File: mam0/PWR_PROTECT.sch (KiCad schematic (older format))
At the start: 4 parts

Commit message: готова схема, требуется проверка
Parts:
- added C? (x4): Конденсатор_керамический, N_RLC:Конденсатор_SMD_0603, symbol elements:Конденсатор_керамический
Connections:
- net GND_OUT: now also C?.2, C?.2, C?.2, C?.2
- net V_OUT: now also C?.1, C?.1, C?.1, C?.1
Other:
- note added: "На интерфейс RS485"
- note added: "На микроконтроллер (AVCC)"
- note added: "На микроконтроллер (VCC)"
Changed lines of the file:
@@
 EESchema Schematic File Version 4
+LIBS:mam0-cache
 EELAYER 29 0
 EELAYER END
 $Descr A4 11693 8268
 encoding utf-8
-Sheet 2 2
+Sheet 2 3
 Title ""
 Date ""
@@
 Wire Wire Line
 	5750 3250 5750 3000
-Text HLabel 6250 2500 2    50   Input ~ 0
+Text HLabel 9000 2500 2    50   Input ~ 0
 V_OUT
 Wire Wire Line
-	5750 2500 6250 2500
+	5750 2500 6500 2500
 Connection ~ 5750 2500
-Text HLabel 6250 3250 2    50   Input ~ 0
+Text HLabel 9000 3250 2    50   Input ~ 0
 GND_OUT
-Wire Wire Line
-	6250 3250 5750 3250
 $Comp
 L elements:Предохранитель FU?
@@
 	4750 3250 4500 3250
 Connection ~ 4500 3250
+$Comp
+L elements:Конденсатор_керамический C?
+U 1 1 5DBC916F
+P 6500 2800
+AR Path="/5DBC916F" Ref="C?"  Part="1"
+AR Path="/5DB9AA7C/5DBC916F" Ref="C?"  Part="1"
+F 0 "C?" V 6450 2950 60  0000 C CNN
+F 1 "Конденсатор_керамический" H 6600 2700 60  0001 C CNN
+F 2 "N_RLC:Конденсатор_SMD_0603" H 6500 2800 60  0001 C CNN
+F 3 "" H 6500 2800 60  0001 C CNN
+F 4 "10 мкФ/6,3 В" V 6650 3100 50  0000 C CNN "Номинал"
+F 5 "С111" H 6500 2800 50  0001 C CNN "УГО"
+	1    6500 2800
+	0    1    1    0
+$EndComp
+$Comp
+L elements:Конденсатор_керамический C?
+U 1 1 5DBC91F5
+P 7250 2800
+AR Path="/5DBC91F5" Ref="C?"  Part="1"
+AR Path="/5DB9AA7C/5DBC91F5" Ref="C?"  Part="1"
+F 0 "C?" V 7200 2950 60  0000 C CNN
+F 1 "Конденсатор_керамический" H 7350 2700 60  0001 C CNN
+F 2 "N_RLC:Конденсатор_SMD_0603" H 7250 2800 60  0001 C CNN
+F 3 "" H 7250 2800 60  0001 C CNN
+F 4 "10 мкФ/6,3 В" V 7400 3100 50  0000 C CNN "Номинал"
+F 5 "С111" H 7250 2800 50  0001 C CNN "УГО"
+	1    7250 2800
+	0    1    1    0
+$EndComp
+Wire Wire Line
+	6500 2750 6500 2500
+Connection ~ 6500 2500
+Wire Wire Line
+	6500 2500 7250 2500
+Wire Wire Line
+	7250 2750 7250 2500
+Wire Wire Line
+	7250 2900 7250 3250
+Wire Wire Line
+	7250 3250 6500 3250
+Wire Wire Line
+	6500 2900 6500 3250
+Connection ~ 6500 3250
+Wire Wire Line
+	6500 3250 5750 3250
+Text Notes 6500 2450 1    50   ~ 0
+На микроконтроллер (VCC)
+Text Notes 7250 2450 1    50   ~ 0
+На микроконтроллер (VCC)
+Wire Wire Line
+	8750 2500 9000 2500
+Wire Wire Line
+	8750 3250 9000 3250
+$Comp
+L elements:Конденсатор_керамический C?
+U 1 1 5DC347F0
+P 8000 2800
+AR Path="/5DC347F0" Ref="C?"  Part="1"
+AR Path="/5DB9AA7C/5DC347F0" Ref="C?"  Part="1"
+F 0 "C?" V 7950 2950 60  0000 C CNN
+F 1 "Конденсатор_керамический" H 8100 2700 60  0001 C CNN
+F 2 "N_RLC:Конденсатор_SMD_0603" H 8000 2800 60  0001 C CNN
+F 3 "" H 8000 2800 60  0001 C CNN
+F 4 "10 мкФ/6,3 В" V 8150 3100 50  0000 C CNN "Номинал"
+F 5 "С111" H 8000 2800 50  0001 C CNN "УГО"
+	1    8000 2800
+	0    1    1    0
+$EndComp
+Wire Wire Line
+	8000 2750 8000 2500
+Wire Wire Line
+	8000 2900 8000 3250
+Wire Wire Line
+	8000 2500 7250 2500
+Connection ~ 7250 2500
+Wire Wire Line
+	7250 3250 8000 3250
+Connection ~ 7250 3250
+Text Notes 8000 2450 1    50   ~ 0
+На микроконтроллер (AVCC)
+$Comp
+L elements:Конденсатор_керамический C?
+U 1 1 5DC60698
+P 8750 2800
+AR Path="/5DC60698" Ref="C?"  Part="1"
+AR Path="/5DB9AA7C/5DC60698" Ref="C?"  Part="1"
+F 0 "C?" V 8700 2950 60  0000 C CNN
+F 1 "Конденсатор_керамический" H 8850 2700 60  0001 C CNN
+F 2 "N_RLC:Конденсатор_SMD_0603" H 8750 2800 60  0001 C CNN
+F 3 "" H 8750 2800 60  0001 C CNN
+F 4 "10 мкФ/6,3 В" V 8900 3100 50  0000 C CNN "Номинал"
+F 5 "С111" H 8750 2800 50  0001 C CNN "УГО"
+	1    8750 2800
+	0    1    1    0
+$EndComp
+Wire Wire Line
+	8750 2750 8750 2500
+Wire Wire Line
+	8750 2900 8750 3250
+Wire Wire Line
+	8750 2500 8000 2500
+Connection ~ 8750 2500
+Connection ~ 8000 2500
+Wire Wire Line
+	8000 3250 8750 3250
+Connection ~ 8000 3250
+Connection ~ 8750 3250
+Text Notes 8750 2450 1    50   ~ 0
+На интерфейс RS485
 $EndSCHEMATC

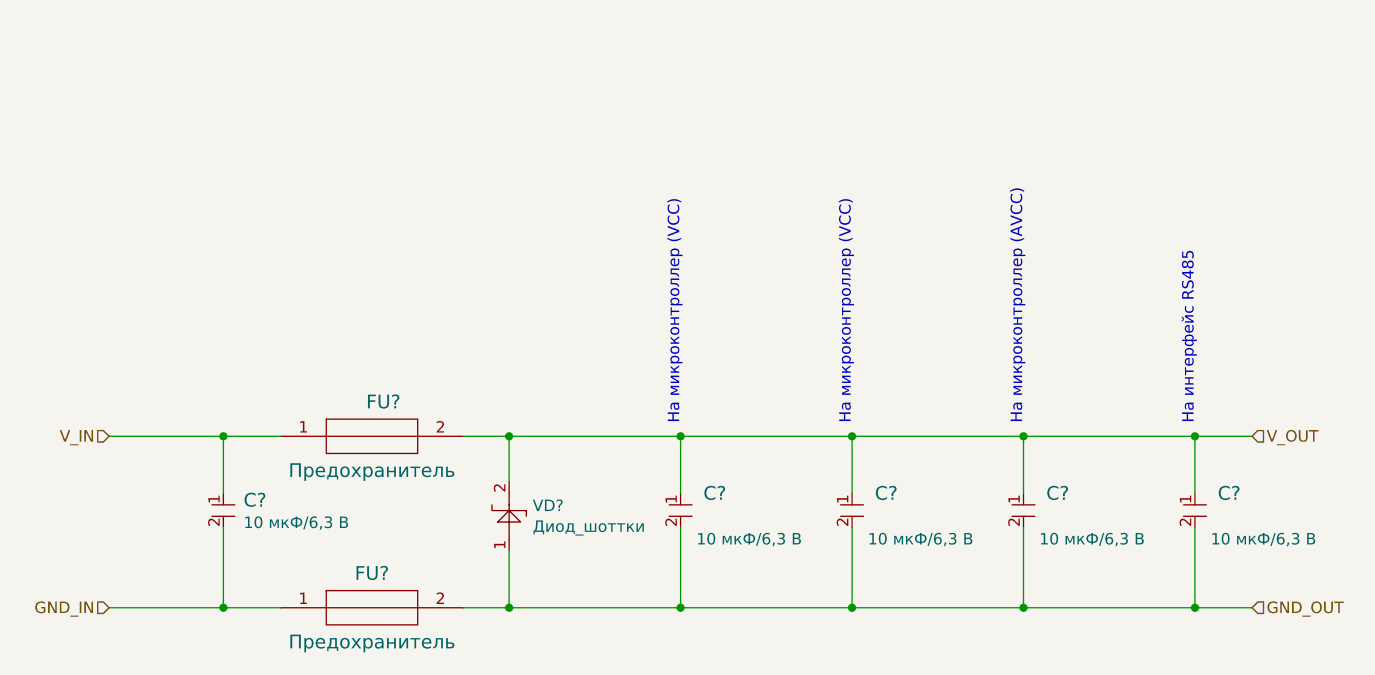
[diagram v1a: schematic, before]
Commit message: начата трассировка
сильно упрощенная схема
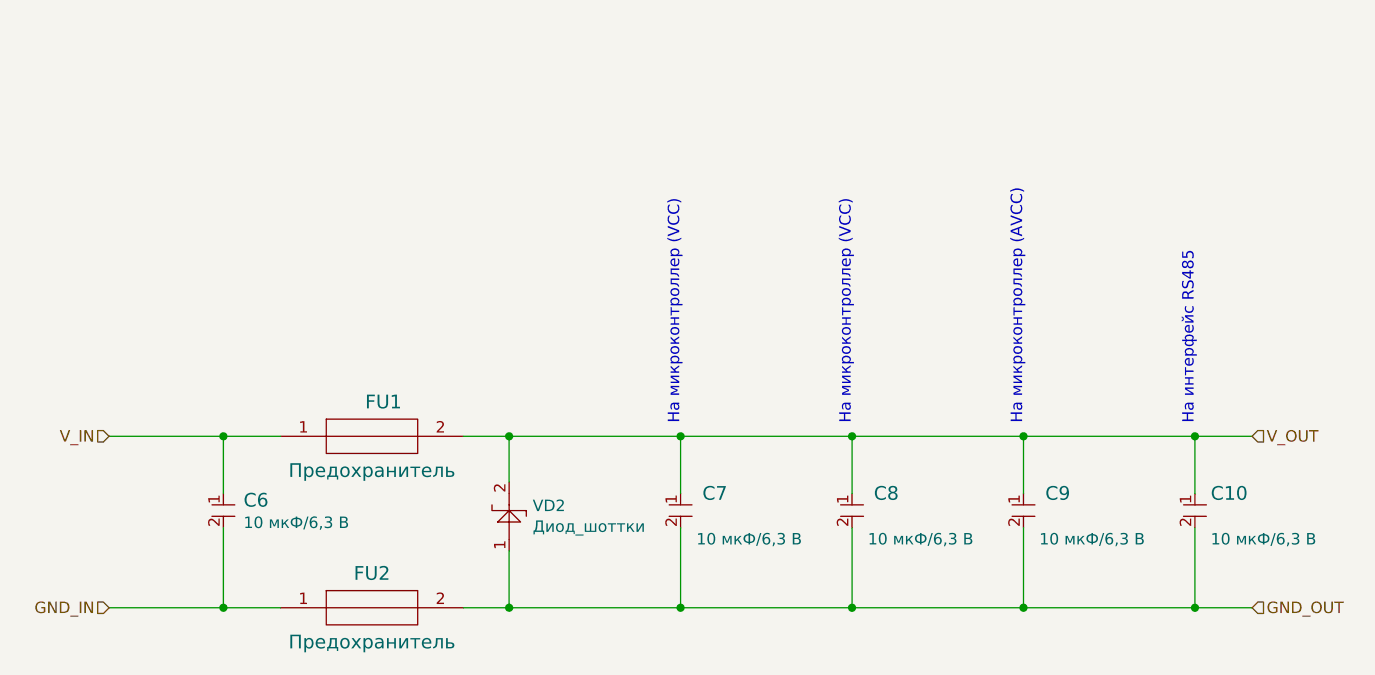
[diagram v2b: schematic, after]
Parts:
- gave numbers to parts that had none: 8
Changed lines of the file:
@@
 P 5150 2500
 AR Path="/5DB9C847" Ref="FU?"  Part="1"
-AR Path="/5DB9AA7C/5DB9C847" Ref="FU?"  Part="1"
-F 0 "FU?" H 5200 2650 60  0000 C CNN
+AR Path="/5DB9AA7C/5DB9C847" Ref="FU1"  Part="1"
+F 0 "FU1" H 5200 2650 60  0000 C CNN
 F 1 "Предохранитель" H 5150 2350 60  0000 C CNN
 F 2 "N_RLC:Предохранитель_SMD_1812" H 5150 2500 60  0001 C CNN
@@
 P 5750 3000
 AR Path="/5DB9C84D" Ref="VD?"  Part="1"
-AR Path="/5DB9AA7C/5DB9C84D" Ref="VD?"  Part="1"
-F 0 "VD?" V 5946 2897 50  0000 R CNN
+AR Path="/5DB9AA7C/5DB9C84D" Ref="VD2"  Part="1"
+F 0 "VD2" V 5946 2897 50  0000 R CNN
 F 1 "Диод_шоттки" V 5855 2897 50  0000 R CNN
 F 2 "N_VD_HL:Диод_S13_SOD-123" H 5650 3000 50  0001 C CNN
@@
 P 4500 2800
 AR Path="/5DB9C855" Ref="C?"  Part="1"
-AR Path="/5DB9AA7C/5DB9C855" Ref="C?"  Part="1"
-F 0 "C?" V 4480 2888 60  0000 L CNN
+AR Path="/5DB9AA7C/5DB9C855" Ref="C6"  Part="1"
+F 0 "C6" V 4480 2888 60  0000 L CNN
 F 1 "Конденсатор_керамический" H 4600 2700 60  0001 C CNN
 F 2 "N_RLC:Конденсатор_SMD_0603" H 4500 2800 60  0001 C CNN
@@
 P 5150 3250
 AR Path="/5DB9F8E1" Ref="FU?"  Part="1"
-AR Path="/5DB9AA7C/5DB9F8E1" Ref="FU?"  Part="1"
-F 0 "FU?" H 5150 3400 60  0000 C CNN
+AR Path="/5DB9AA7C/5DB9F8E1" Ref="FU2"  Part="1"
+F 0 "FU2" H 5150 3400 60  0000 C CNN
 F 1 "Предохранитель" H 5150 3100 60  0000 C CNN
 F 2 "N_RLC:Предохранитель_SMD_1812" H 5150 3250 60  0001 C CNN
@@
 P 6500 2800
 AR Path="/5DBC916F" Ref="C?"  Part="1"
-AR Path="/5DB9AA7C/5DBC916F" Ref="C?"  Part="1"
-F 0 "C?" V 6450 2950 60  0000 C CNN
+AR Path="/5DB9AA7C/5DBC916F" Ref="C7"  Part="1"
+F 0 "C7" V 6450 2950 60  0000 C CNN
 F 1 "Конденсатор_керамический" H 6600 2700 60  0001 C CNN
 F 2 "N_RLC:Конденсатор_SMD_0603" H 6500 2800 60  0001 C CNN
@@
 P 7250 2800
 AR Path="/5DBC91F5" Ref="C?"  Part="1"
-AR Path="/5DB9AA7C/5DBC91F5" Ref="C?"  Part="1"
-F 0 "C?" V 7200 2950 60  0000 C CNN
+AR Path="/5DB9AA7C/5DBC91F5" Ref="C8"  Part="1"
+F 0 "C8" V 7200 2950 60  0000 C CNN
 F 1 "Конденсатор_керамический" H 7350 2700 60  0001 C CNN
 F 2 "N_RLC:Конденсатор_SMD_0603" H 7250 2800 60  0001 C CNN
@@
 P 8000 2800
 AR Path="/5DC347F0" Ref="C?"  Part="1"
-AR Path="/5DB9AA7C/5DC347F0" Ref="C?"  Part="1"
-F 0 "C?" V 7950 2950 60  0000 C CNN
+AR Path="/5DB9AA7C/5DC347F0" Ref="C9"  Part="1"
+F 0 "C9" V 7950 2950 60  0000 C CNN
 F 1 "Конденсатор_керамический" H 8100 2700 60  0001 C CNN
 F 2 "N_RLC:Конденсатор_SMD_0603" H 8000 2800 60  0001 C CNN
@@
 P 8750 2800
 AR Path="/5DC60698" Ref="C?"  Part="1"
-AR Path="/5DB9AA7C/5DC60698" Ref="C?"  Part="1"
-F 0 "C?" V 8700 2950 60  0000 C CNN
+AR Path="/5DB9AA7C/5DC60698" Ref="C10"  Part="1"
+F 0 "C10" V 8700 2950 60  0000 C CNN
 F 1 "Конденсатор_керамический" H 8850 2700 60  0001 C CNN
 F 2 "N_RLC:Конденсатор_SMD_0603" H 8750 2800 60  0001 C CNN
